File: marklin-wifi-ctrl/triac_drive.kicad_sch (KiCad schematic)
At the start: 12 parts, among them Q800 BT136-600E, Q801 BT136-600E, U800 MOC3021S-TA1, U801 MOC3021S-TA1

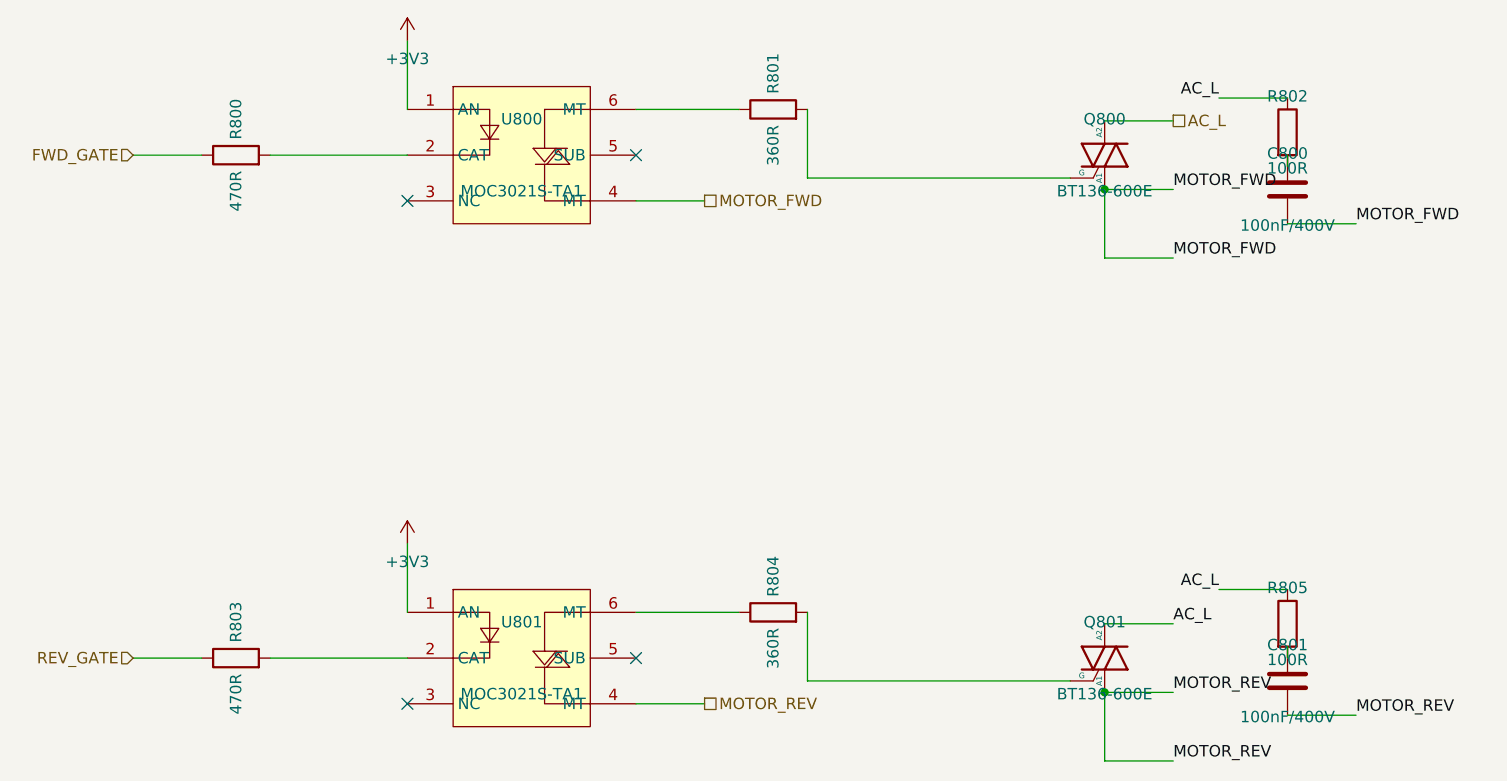
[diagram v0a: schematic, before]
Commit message: Rewrite TRIAC drive to use direct wires instead of net labels
Replace motor net and AC_L net labels with direct wire connections
between MOC pin4, TRIAC, and snubber components. Only AC_L net label
on second channel remains (one hlabel per sheet rule).

Co-Authored-By: Claude Opus 4.6 <noreply@anthropic.com>
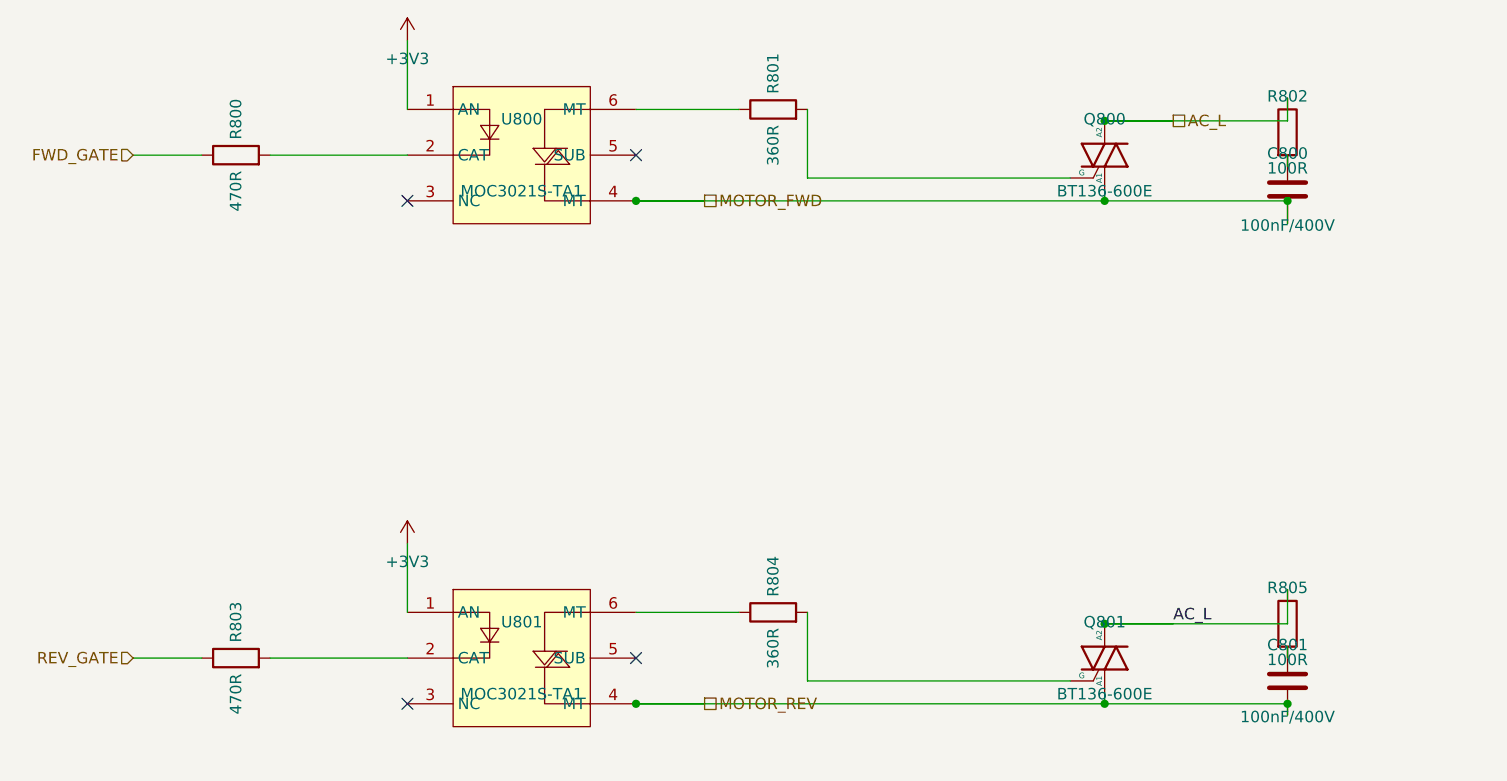
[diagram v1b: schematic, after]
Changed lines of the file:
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@@
 	)
 	(wire
-		(pts (xy 144.78 58.42) (xy 152.4 58.42))
-		(stroke (width 0) (type solid))
-	)
-	(label "MOTOR_FWD"
-		(at 152.4 58.42 0)
-		(fields_autoplaced yes)
-		(effects (font (size 1.27 1.27)) (justify left bottom))
+		(pts (xy 92.71 59.69) (xy 144.78 59.69))
+		(stroke (width 0) (type solid))
+	)
+	(wire
+		(pts (xy 144.78 59.69) (xy 144.78 58.42))
+		(stroke (width 0) (type solid))
+	)
+	(junction
+		(at 92.71 59.69)
+		(diameter 0)
+		(color 0 0 0 0)
 	)
 	(wire
@@
 		(effects (font (size 1.27 1.27)) (justify left bottom))
 	)
-	(wire
-		(pts (xy 144.78 58.42) (xy 144.78 66.04))
-		(stroke (width 0) (type solid))
-	)
-	(wire
-		(pts (xy 144.78 66.04) (xy 152.4 66.04))
-		(stroke (width 0) (type solid))
-	)
-	(label "MOTOR_FWD"
-		(at 152.4 66.04 0)
-		(fields_autoplaced yes)
-		(effects (font (size 1.27 1.27)) (justify left bottom))
-	)
-	(junction
-		(at 144.78 58.42)
-		(diameter 0)
-		(color 0 0 0 0)
-	)
 	(symbol
 		(lib_id "Device:R")
@@
 	)
 	(wire
-		(pts (xy 157.48 48.26) (xy 165.1 48.26))
-		(stroke (width 0) (type solid))
-	)
-	(label "AC_L"
-		(at 157.48 48.26 180)
-		(fields_autoplaced yes)
-		(effects (font (size 1.27 1.27)) (justify right bottom))
-	)
-	(wire
-		(pts (xy 165.1 62.23) (xy 172.72 62.23))
-		(stroke (width 0) (type solid))
-	)
-	(label "MOTOR_FWD"
-		(at 172.72 62.23 0)
-		(fields_autoplaced yes)
-		(effects (font (size 1.27 1.27)) (justify left bottom))
+		(pts (xy 144.78 50.8) (xy 165.1 50.8))
+		(stroke (width 0) (type solid))
+	)
+	(wire
+		(pts (xy 165.1 50.8) (xy 165.1 48.26))
+		(stroke (width 0) (type solid))
+	)
+	(junction
+		(at 144.78 50.8)
+		(diameter 0)
+		(color 0 0 0 0)
+	)
+	(wire
+		(pts (xy 144.78 59.69) (xy 165.1 59.69))
+		(stroke (width 0) (type solid))
+	)
+	(wire
+		(pts (xy 165.1 59.69) (xy 165.1 62.23))
+		(stroke (width 0) (type solid))
+	)
+	(junction
+		(at 144.78 59.69)
+		(diameter 0)
+		(color 0 0 0 0)
+	)
+	(junction
+		(at 165.1 59.69)
+		(diameter 0)
+		(color 0 0 0 0)
 	)
 	(symbol
@@
 	)
 	(wire
-		(pts (xy 144.78 114.3) (xy 152.4 114.3))
-		(stroke (width 0) (type solid))
-	)
-	(label "MOTOR_REV"
-		(at 152.4 114.3 0)
-		(fields_autoplaced yes)
-		(effects (font (size 1.27 1.27)) (justify left bottom))
+		(pts (xy 92.71 115.57) (xy 144.78 115.57))
+		(stroke (width 0) (type solid))
+	)
+	(wire
+		(pts (xy 144.78 115.57) (xy 144.78 114.3))
+		(stroke (width 0) (type solid))
+	)
+	(junction
+		(at 92.71 115.57)
+		(diameter 0)
+		(color 0 0 0 0)
 	)
 	(wire
@@
 		(effects (font (size 1.27 1.27)) (justify left bottom))
 	)
-	(wire
-		(pts (xy 144.78 114.3) (xy 144.78 121.92))
-		(stroke (width 0) (type solid))
-	)
-	(wire
-		(pts (xy 144.78 121.92) (xy 152.4 121.92))
-		(stroke (width 0) (type solid))
-	)
-	(label "MOTOR_REV"
-		(at 152.4 121.92 0)
-		(fields_autoplaced yes)
-		(effects (font (size 1.27 1.27)) (justify left bottom))
-	)
-	(junction
-		(at 144.78 114.3)
-		(diameter 0)
-		(color 0 0 0 0)
-	)
 	(symbol
 		(lib_id "Device:R")
@@
 	)
 	(wire
-		(pts (xy 157.48 102.87) (xy 165.1 102.87))
-		(stroke (width 0) (type solid))
-	)
-	(label "AC_L"
-		(at 157.48 102.87 180)
-		(fields_autoplaced yes)
-		(effects (font (size 1.27 1.27)) (justify right bottom))
-	)
-	(wire
-		(pts (xy 165.1 116.84) (xy 172.72 116.84))
-		(stroke (width 0) (type solid))
-	)
-	(label "MOTOR_REV"
-		(at 172.72 116.84 0)
-		(fields_autoplaced yes)
-		(effects (font (size 1.27 1.27)) (justify left bottom))
+		(pts (xy 144.78 106.68) (xy 165.1 106.68))
+		(stroke (width 0) (type solid))
+	)
+	(wire
+		(pts (xy 165.1 106.68) (xy 165.1 102.87))
+		(stroke (width 0) (type solid))
+	)
+	(junction
+		(at 144.78 106.68)
+		(diameter 0)
+		(color 0 0 0 0)
+	)
+	(wire
+		(pts (xy 144.78 115.57) (xy 165.1 115.57))
+		(stroke (width 0) (type solid))
+	)
+	(wire
+		(pts (xy 165.1 115.57) (xy 165.1 116.84))
+		(stroke (width 0) (type solid))
+	)
+	(junction
+		(at 144.78 115.57)
+		(diameter 0)
+		(color 0 0 0 0)
+	)
+	(junction
+		(at 165.1 115.57)
+		(diameter 0)
+		(color 0 0 0 0)
 	)
 	(sheet_instances

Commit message: Fix TRIAC drive: route wires outside components, move output hlabels to rightmost symbols
Snubber wires now route around R_sn/C_sn bodies instead of through them.
Output hlabels (AC_L, MOTOR_FWD/REV) moved to snubber pins (rightmost symbols).
Added drawing rules to CLAUDE.md and SKILL.md.

Co-Authored-By: Claude Opus 4.6 <noreply@anthropic.com>
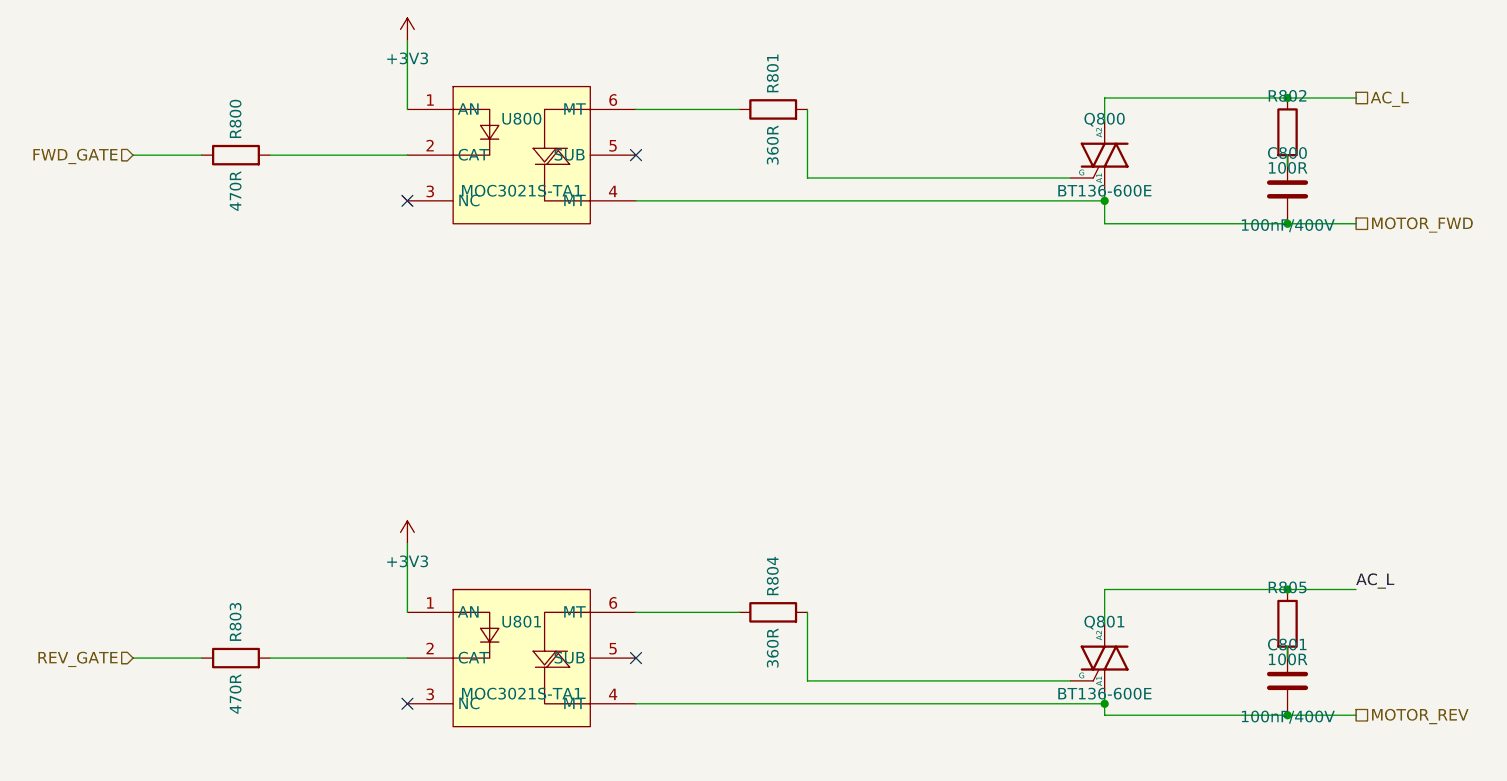
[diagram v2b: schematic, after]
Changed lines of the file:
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@@
-	)
-	(wire
-		(pts (xy 92.71 59.69) (xy 100.33 59.69))
-		(stroke (width 0) (type solid))
-	)
-	(hierarchical_label "MOTOR_FWD"
-		(shape passive)
-		(at 100.33 59.69 0)
-		(fields_autoplaced yes)
-		(effects (font (size 1.27 1.27)) (justify left bottom))
 	)
 	(wire
@@
 		(pts (xy 144.78 59.69) (xy 144.78 58.42))
 		(stroke (width 0) (type solid))
-	)
-	(junction
-		(at 92.71 59.69)
-		(diameter 0)
-		(color 0 0 0 0)
-	)
-	(wire
-		(pts (xy 144.78 50.8) (xy 152.4 50.8))
-		(stroke (width 0) (type solid))
-	)
-	(hierarchical_label "AC_L"
-		(shape passive)
-		(at 152.4 50.8 0)
-		(fields_autoplaced yes)
-		(effects (font (size 1.27 1.27)) (justify left bottom))
 	)
 	(symbol
@@
 	)
 	(wire
-		(pts (xy 144.78 50.8) (xy 165.1 50.8))
-		(stroke (width 0) (type solid))
-	)
-	(wire
-		(pts (xy 165.1 50.8) (xy 165.1 48.26))
-		(stroke (width 0) (type solid))
-	)
-	(junction
-		(at 144.78 50.8)
-		(diameter 0)
-		(color 0 0 0 0)
-	)
-	(wire
-		(pts (xy 144.78 59.69) (xy 165.1 59.69))
-		(stroke (width 0) (type solid))
-	)
-	(wire
-		(pts (xy 165.1 59.69) (xy 165.1 62.23))
+		(pts (xy 144.78 50.8) (xy 144.78 48.26))
+		(stroke (width 0) (type solid))
+	)
+	(wire
+		(pts (xy 144.78 48.26) (xy 165.1 48.26))
+		(stroke (width 0) (type solid))
+	)
+	(wire
+		(pts (xy 144.78 59.69) (xy 144.78 62.23))
+		(stroke (width 0) (type solid))
+	)
+	(wire
+		(pts (xy 144.78 62.23) (xy 165.1 62.23))
 		(stroke (width 0) (type solid))
 	)
@@
 		(color 0 0 0 0)
 	)
+	(wire
+		(pts (xy 165.1 48.26) (xy 172.72 48.26))
+		(stroke (width 0) (type solid))
+	)
+	(hierarchical_label "AC_L"
+		(shape passive)
+		(at 172.72 48.26 0)
+		(fields_autoplaced yes)
+		(effects (font (size 1.27 1.27)) (justify left bottom))
+	)
 	(junction
-		(at 165.1 59.69)
+		(at 165.1 48.26)
+		(diameter 0)
+		(color 0 0 0 0)
+	)
+	(wire
+		(pts (xy 165.1 62.23) (xy 172.72 62.23))
+		(stroke (width 0) (type solid))
+	)
+	(hierarchical_label "MOTOR_FWD"
+		(shape passive)
+		(at 172.72 62.23 0)
+		(fields_autoplaced yes)
+		(effects (font (size 1.27 1.27)) (justify left bottom))
+	)
+	(junction
+		(at 165.1 62.23)
 		(diameter 0)
 		(color 0 0 0 0)
@@
 	)
 	(wire
-		(pts (xy 92.71 115.57) (xy 100.33 115.57))
-		(stroke (width 0) (type solid))
-	)
-	(hierarchical_label "MOTOR_REV"
-		(shape passive)
-		(at 100.33 115.57 0)
-		(fields_autoplaced yes)
-		(effects (font (size 1.27 1.27)) (justify left bottom))
-	)
-	(wire
 		(pts (xy 92.71 115.57) (xy 144.78 115.57))
 		(stroke (width 0) (type solid))
@@
 		(pts (xy 144.78 115.57) (xy 144.78 114.3))
 		(stroke (width 0) (type solid))
-	)
-	(junction
-		(at 92.71 115.57)
-		(diameter 0)
-		(color 0 0 0 0)
-	)
-	(wire
-		(pts (xy 144.78 106.68) (xy 152.4 106.68))
-		(stroke (width 0) (type solid))
-	)
-	(label "AC_L"
-		(at 152.4 106.68 0)
-		(fields_autoplaced yes)
-		(effects (font (size 1.27 1.27)) (justify left bottom))
 	)
 	(symbol
@@
 	)
 	(wire
-		(pts (xy 144.78 106.68) (xy 165.1 106.68))
-		(stroke (width 0) (type solid))
-	)
-	(wire
-		(pts (xy 165.1 106.68) (xy 165.1 102.87))
-		(stroke (width 0) (type solid))
-	)
-	(junction
-		(at 144.78 106.68)
-		(diameter 0)
-		(color 0 0 0 0)
-	)
-	(wire
-		(pts (xy 144.78 115.57) (xy 165.1 115.57))
-		(stroke (width 0) (type solid))
-	)
-	(wire
-		(pts (xy 165.1 115.57) (xy 165.1 116.84))
+		(pts (xy 144.78 106.68) (xy 144.78 102.87))
+		(stroke (width 0) (type solid))
+	)
+	(wire
+		(pts (xy 144.78 102.87) (xy 165.1 102.87))
+		(stroke (width 0) (type solid))
+	)
+	(wire
+		(pts (xy 144.78 115.57) (xy 144.78 116.84))
+		(stroke (width 0) (type solid))
+	)
+	(wire
+		(pts (xy 144.78 116.84) (xy 165.1 116.84))
 		(stroke (width 0) (type solid))
 	)
@@
 		(color 0 0 0 0)
 	)
+	(wire
+		(pts (xy 165.1 102.87) (xy 172.72 102.87))
+		(stroke (width 0) (type solid))
+	)
+	(label "AC_L"
+		(at 172.72 102.87 0)
+		(fields_autoplaced yes)
+		(effects (font (size 1.27 1.27)) (justify left bottom))
+	)
 	(junction
-		(at 165.1 115.57)
+		(at 165.1 102.87)
 		(diameter 0)
 		(color 0 0 0 0)
+	)
+	(wire
+		(pts (xy 165.1 116.84) (xy 172.72 116.84))
+		(stroke (width 0) (type solid))
+	)
+	(hierarchical_label "MOTOR_REV"
+		(shape passive)
+		(at 172.72 116.84 0)
+		(fields_autoplaced yes)
+		(effects (font (size 1.27 1.27)) (justify left bottom))
+	)
+	(junction
+		(at 165.1 116.84)
+		(diameter 0)
+		(color 0 0 0 0)
